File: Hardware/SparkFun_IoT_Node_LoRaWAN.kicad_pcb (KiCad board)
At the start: 4 copper layers, 59 x 82 mm, 102 parts, among them J1 Conn_01x03, J2 JST_2mm_LiPo, J3 Qwiic_RA, J4 USB_C_Receptacle, J5 USB_C_Receptacle, J6 SWD, J7 Conn_01x12, J8 Conn_01x12, J9 microSD_Friction, SW1 SMD_4.6x2.8mm_h2.5mm, SW2 SMD_4.6x2.8mm_h2.5mm, SW3 DPDT_Slide_SMD_7.2x3.5mm, SW4 PTH_RA_h7.5mm, U3 CH340C, U4 W25Q128JVPIM, U5 LM66200, U6 RT9080-3.3, U7 MCP73831, U8 MAX17048, U9 RT9080-3.3

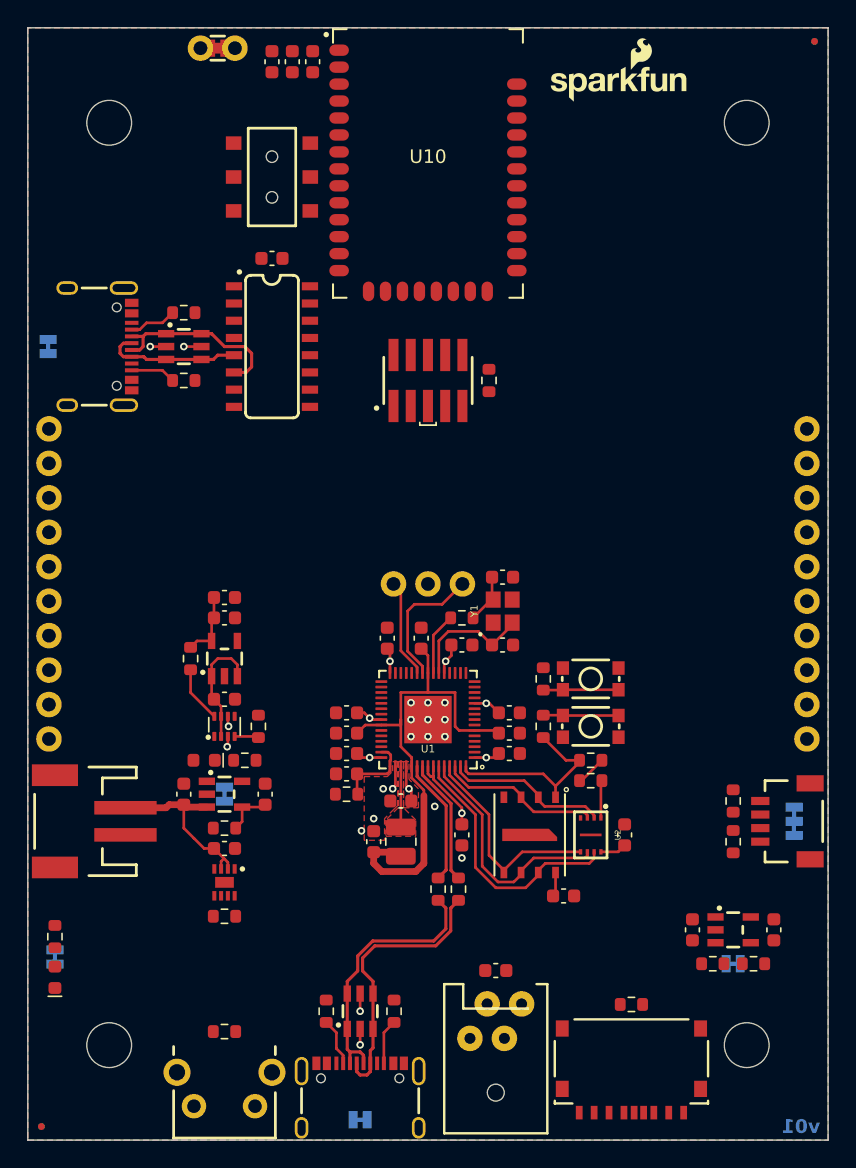
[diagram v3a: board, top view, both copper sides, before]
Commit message: Finish connections and routing
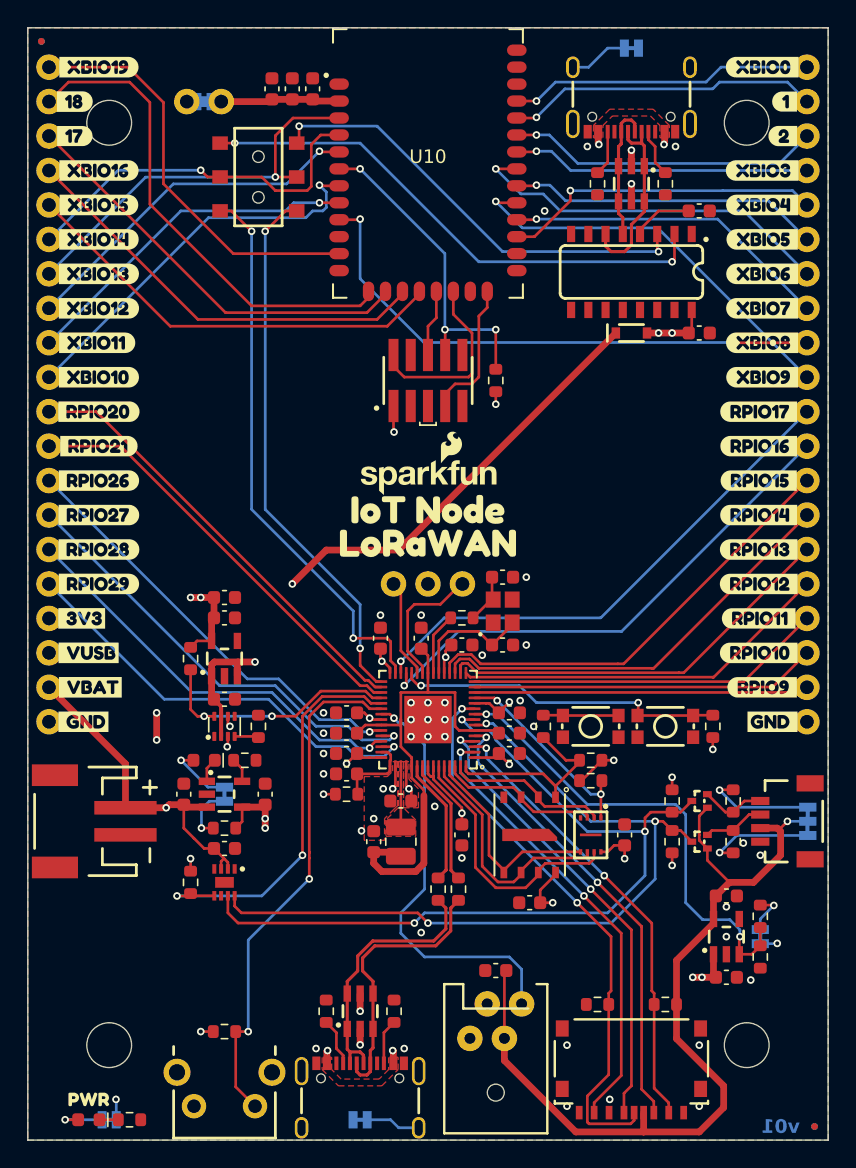
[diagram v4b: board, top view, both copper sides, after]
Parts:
- added C31: 0.1uF, SparkFun-Capacitor:C_0603_1608Metric, F.Cu at (120.0, 81.5)
- added D6: BAT20J, SparkFun-Semiconductor-Standard:SOD-323, F.Cu at (115.0, 81.5)
- added G***: LOGO, SparkFun-Aesthetic:SparkFun_Logo_10mm, B.Cu at (100.0, 85.0)
- added Q1: RE1C002UNTCL, SparkFun-Semiconductor-Standard:SC-89 SOT-490, F.Cu at (119.5, 119.0)
- added Q2: RE1C002UNTCL, SparkFun-Semiconductor-Standard:SC-89 SOT-490, F.Cu at (119.5, 116.0)
- added R26: 10k, SparkFun-Resistor:R_0603_1608Metric, F.Cu at (117.5, 131.0)
- added R27: 2.2k, SparkFun-Resistor:R_0603_1608Metric, F.Cu at (118.0, 116.0)
- added R28: 2.2k, SparkFun-Resistor:R_0603_1608Metric, F.Cu at (118.0, 119.0)
- added kibuzzard-6691B276: G***, kibuzzard-6691B276, F.Cu at (74.6, 110.2)
- added kibuzzard-6691B276: G***, kibuzzard-6691B276, B.Cu at (125.4, 110.2)
- added kibuzzard-6691B276: G***, kibuzzard-6691B276, B.Cu at (100.0, 97.5)
- added kibuzzard-6691B296: G***, kibuzzard-6691B296, F.Cu at (75.1, 107.6)
- added kibuzzard-6691B29E: G***, kibuzzard-6691B29E, F.Cu at (75.0, 105.1)
- added kibuzzard-6691B2AD: G***, kibuzzard-6691B2AD, F.Cu at (74.5, 102.5)
- added kibuzzard-6691B2C0: G***, kibuzzard-6691B2C0, F.Cu at (75.7, 100.0)
- added kibuzzard-6691B2FA: G***, kibuzzard-6691B2FA, F.Cu at (75.7, 97.5)
- added kibuzzard-6691B2FE: G***, kibuzzard-6691B2FE, F.Cu at (75.7, 94.9)
- added kibuzzard-6691B304: G***, kibuzzard-6691B304, F.Cu at (75.7, 92.4)
- added kibuzzard-6691B307: G***, kibuzzard-6691B307, F.Cu at (75.7, 89.8)
- added kibuzzard-6691B30B: G***, kibuzzard-6691B30B, F.Cu at (75.7, 87.3)
- added kibuzzard-6691B338: G***, kibuzzard-6691B338, F.Cu at (124.4, 87.3)
- added kibuzzard-6691B363: G***, kibuzzard-6691B363, F.Cu at (124.4, 100.0)
- added kibuzzard-6691B36B: G***, kibuzzard-6691B36B, F.Cu at (124.4, 89.8)
- added kibuzzard-6691B36F: G***, kibuzzard-6691B36F, F.Cu at (124.4, 92.4)
- added kibuzzard-6691B376: G***, kibuzzard-6691B376, F.Cu at (124.4, 94.9)
- added kibuzzard-6691B37B: G***, kibuzzard-6691B37B, F.Cu at (124.4, 97.5)
- added kibuzzard-6691B383: G***, kibuzzard-6691B383, F.Cu at (124.4, 102.5)
- added kibuzzard-6691B387: G***, kibuzzard-6691B387, F.Cu at (124.4, 105.1)
- added kibuzzard-6691B38E: G***, kibuzzard-6691B38E, F.Cu at (124.6, 107.6)
- added kibuzzard-6691B3A2: G***, kibuzzard-6691B3A2, F.Cu at (125.4, 110.2)
- added kibuzzard-6691B3A2: G***, kibuzzard-6691B3A2, B.Cu at (74.6, 110.2)
- added kibuzzard-6691B3CB: G***, kibuzzard-6691B3CB, F.Cu at (75.7, 84.8)
- added kibuzzard-6691B3E1: G***, kibuzzard-6691B3E1, F.Cu at (75.7, 61.9)
- added kibuzzard-6691B3E7: G***, kibuzzard-6691B3E7, F.Cu at (75.7, 69.5)
- added kibuzzard-6691B3EC: G***, kibuzzard-6691B3EC, F.Cu at (75.7, 72.1)
- added kibuzzard-6691B3F1: G***, kibuzzard-6691B3F1, F.Cu at (75.7, 74.6)
- added kibuzzard-6691B3F5: G***, kibuzzard-6691B3F5, F.Cu at (75.7, 77.1)
- added kibuzzard-6691B3F9: G***, kibuzzard-6691B3F9, F.Cu at (75.7, 79.7)
- added kibuzzard-6691B3FD: G***, kibuzzard-6691B3FD, F.Cu at (75.6, 82.2)
- added kibuzzard-6691B419: G***, kibuzzard-6691B419, F.Cu at (124.6, 84.8)
- added kibuzzard-6691B436: G***, kibuzzard-6691B436, F.Cu at (124.6, 61.9)
- added kibuzzard-6691B43C: G***, kibuzzard-6691B43C, F.Cu at (124.6, 69.5)
- added kibuzzard-6691B440: G***, kibuzzard-6691B440, F.Cu at (124.6, 72.1)
- added kibuzzard-6691B444: G***, kibuzzard-6691B444, F.Cu at (124.6, 74.6)
- added kibuzzard-6691B448: G***, kibuzzard-6691B448, F.Cu at (124.6, 77.1)
- added kibuzzard-6691B44C: G***, kibuzzard-6691B44C, F.Cu at (124.6, 79.7)
- added kibuzzard-6691B450: G***, kibuzzard-6691B450, F.Cu at (124.6, 82.2)
- added kibuzzard-6691B464: G***, kibuzzard-6691B464, F.Cu at (126.2, 67.0)
- added kibuzzard-6691B472: G***, kibuzzard-6691B472, F.Cu at (126.3, 64.4)
- added kibuzzard-6691B480: G***, kibuzzard-6691B480, F.Cu at (74.0, 67.0)
- added kibuzzard-6691B48E: G***, kibuzzard-6691B48E, F.Cu at (74.0, 64.4)
- added kibuzzard-6691B4B8: G***, kibuzzard-6691B4B8, F.Cu at (100.0, 94.5)
- added kibuzzard-6691B4B8: G***, kibuzzard-6691B4B8, B.Cu at (100.0, 87.5)
- added kibuzzard-6691B4CC: G***, kibuzzard-6691B4CC, F.Cu at (100.0, 97.0)
- added kibuzzard-6691B4CC: G***, kibuzzard-6691B4CC, B.Cu at (100.0, 90.0)
- added kibuzzard-6691B525: G***, kibuzzard-6691B525, B.Cu at (75.7, 87.3)
- added kibuzzard-6691B54A: G***, kibuzzard-6691B54A, B.Cu at (75.7, 89.8)
- added kibuzzard-6691B55C: G***, kibuzzard-6691B55C, B.Cu at (75.7, 92.4)
- added kibuzzard-6691B561: G***, kibuzzard-6691B561, B.Cu at (75.7, 94.9)
- added kibuzzard-6691B566: G***, kibuzzard-6691B566, B.Cu at (75.7, 97.5)
- added kibuzzard-6691B56B: G***, kibuzzard-6691B56B, B.Cu at (75.7, 100.0)
- added kibuzzard-6691B580: G***, kibuzzard-6691B580, B.Cu at (124.4, 87.3)
- added kibuzzard-6691B59B: G***, kibuzzard-6691B59B, B.Cu at (124.6, 107.6)
- added kibuzzard-6691B5A1: G***, kibuzzard-6691B5A1, B.Cu at (124.4, 105.1)
- added kibuzzard-6691B5A6: G***, kibuzzard-6691B5A6, B.Cu at (124.4, 102.5)
- added kibuzzard-6691B5AC: G***, kibuzzard-6691B5AC, B.Cu at (124.4, 100.0)
- added kibuzzard-6691B5B1: G***, kibuzzard-6691B5B1, B.Cu at (124.4, 97.5)
- added kibuzzard-6691B5BB: G***, kibuzzard-6691B5BB, B.Cu at (124.4, 94.9)
- added kibuzzard-6691B5C0: G***, kibuzzard-6691B5C0, B.Cu at (124.4, 92.4)
- added kibuzzard-6691B5C3: G***, kibuzzard-6691B5C3, B.Cu at (124.4, 89.8)
- added kibuzzard-6691B5E6: G***, kibuzzard-6691B5E6, B.Cu at (74.5, 102.5)
- added kibuzzard-6691B5F0: G***, kibuzzard-6691B5F0, B.Cu at (75.0, 105.1)
- added kibuzzard-6691B5FB: G***, kibuzzard-6691B5FB, B.Cu at (75.1, 107.6)
- added kibuzzard-6691B60A: G***, kibuzzard-6691B60A, B.Cu at (124.6, 84.8)
- added kibuzzard-6691B61F: G***, kibuzzard-6691B61F, B.Cu at (124.6, 61.9)
- added kibuzzard-6691B623: G***, kibuzzard-6691B623, B.Cu at (124.6, 69.5)
- added kibuzzard-6691B627: G***, kibuzzard-6691B627, B.Cu at (124.6, 72.1)
- added kibuzzard-6691B62B: G***, kibuzzard-6691B62B, B.Cu at (124.6, 74.6)
- added kibuzzard-6691B62F: G***, kibuzzard-6691B62F, B.Cu at (124.6, 77.1)
- added kibuzzard-6691B633: G***, kibuzzard-6691B633, B.Cu at (124.6, 79.7)
- added kibuzzard-6691B637: G***, kibuzzard-6691B637, B.Cu at (124.6, 82.2)
- added kibuzzard-6691B641: G***, kibuzzard-6691B641, B.Cu at (126.2, 67.0)
- added kibuzzard-6691B649: G***, kibuzzard-6691B649, B.Cu at (126.3, 64.4)
- added kibuzzard-6691B658: G***, kibuzzard-6691B658, B.Cu at (74.0, 67.0)
- added kibuzzard-6691B661: G***, kibuzzard-6691B661, B.Cu at (74.0, 64.4)
- added kibuzzard-6691B670: G***, kibuzzard-6691B670, B.Cu at (75.7, 69.5)
- added kibuzzard-6691B697: G***, kibuzzard-6691B697, B.Cu at (75.7, 61.9)
- added kibuzzard-6691B6A1: G***, kibuzzard-6691B6A1, B.Cu at (75.7, 72.1)
- added kibuzzard-6691B6A6: G***, kibuzzard-6691B6A6, B.Cu at (75.7, 74.6)
- added kibuzzard-6691B6AB: G***, kibuzzard-6691B6AB, B.Cu at (75.7, 77.1)
- added kibuzzard-6691B6B0: G***, kibuzzard-6691B6B0, B.Cu at (75.7, 79.7)
- added kibuzzard-6691B6B5: G***, kibuzzard-6691B6B5, B.Cu at (75.6, 82.2)
- added kibuzzard-6691B6B9: G***, kibuzzard-6691B6B9, B.Cu at (75.7, 84.8)
- added kibuzzard-6691B6EC: G***, kibuzzard-6691B6EC, B.Cu at (83.5, 66.1)
- added kibuzzard-6691B712: G***, kibuzzard-6691B712, B.Cu at (95.0, 137.8)
- added kibuzzard-6691B712: G***, kibuzzard-6691B712, B.Cu at (115.0, 62.2)
- added kibuzzard-6691B72F: G***, kibuzzard-6691B72F, B.Cu at (76.5, 137.8)
- added kibuzzard-6691B73B: G***, kibuzzard-6691B73B, B.Cu at (126.2, 117.5)
- added kibuzzard-6691B750: G***, kibuzzard-6691B750, B.Cu at (126.2, 126.0)
- added kibuzzard-6691B763: G***, kibuzzard-6691B763, B.Cu at (86.8, 115.5)
- added kibuzzard-6691B7AB: G***, kibuzzard-6691B7AB, B.Cu at (102.5, 96.3)
- added kibuzzard-6691B7BF: G***, kibuzzard-6691B7BF, B.Cu at (97.5, 96.4)
- added kibuzzard-6691B872: G***, kibuzzard-6691B872, F.Cu at (75.0, 138.0)
- J7, J8: footprint SparkFun-Connector:1x10 -> SparkFun-Connector:1x20
- JP6: moved to B.Cu
- moved FID1 57.0 mm to (71.5, 60.0)
- moved FID2 57.0 mm to (128.5, 140.0)
- moved FID3 57.0 mm to (71.5, 60.0)
- moved FID4 57.0 mm to (128.5, 140.0)
- moved J7 49.5 mm to (72.1, 61.9), turned to -90 degrees
- moved J8 49.5 mm to (127.9, 61.9), turned to -90 degrees
- moved JP5 48.3 mm to (115.0, 60.5), turned to 0 degrees
- moved J4 39.7 mm to (115.0, 67.0), turned to 180 degrees
- moved R18 36.7 mm to (117.5, 70.5), turned to -90 degrees
- moved D5 35.1 mm to (115.0, 70.5), turned to -90 degrees
- moved R17 33.8 mm to (112.5, 70.5), turned to -90 degrees
- moved G*** 32.2 mm to (100.0, 92.0)
- moved C27 31.7 mm to (120.0, 72.5), turned to 0 degrees
- moved U3 27.1 mm to (115.0, 77.0), turned to -90 degrees
- moved R10 14.6 mm to (78.0, 139.5), turned to 0 degrees
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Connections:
- C27 pad 1: 3.3V -> V3
- C4 pad 1: VBUS -> VUSB
- D3 pad 1: GND -> Net-(D3-K)
- D4 pad 5: VBUS -> VUSB
- D5 pad 5: VBUS -> VUSB_2
- J3 pad 3: SDA -> SDA_OUT
- J3 pad 4: SCL -> SCL_OUT
- J4 pad VBUS: VBUS -> VUSB_2
- J5 pad VBUS: VBUS -> VUSB
- J6 pad 10: XBLR_~{RESET} -> (no net)
- J6 pad 2: XBLR_SWDIO -> XBLR_SWO
- J6 pad 3: GND -> (no net)
- J6 pad 4: XBLR_SWCLK -> (no net)
- J6 pad 6: XBLR_SWO -> XBLR_SWCLK
- J6 pad 7: (no net) -> XBLR_SWDIO
- J6 pad 8: (no net) -> XBLR_~{RESET}
- J6 pad 9: GND -> (no net)
- J7 pad 1: unconnected-(J7-Pin_1-Pad1) -> XBLR_IO19
- J7 pad 10: unconnected-(J7-Pin_10-Pad10) -> XBLR_IO10
- J7 pad 2: unconnected-(J7-Pin_2-Pad2) -> XBLR_IO18
- J7 pad 3: unconnected-(J7-Pin_3-Pad3) -> XBLR_IO17
- J7 pad 4: unconnected-(J7-Pin_4-Pad4) -> XBLR_IO16
- J7 pad 5: unconnected-(J7-Pin_5-Pad5) -> XBLR_IO15
- J7 pad 6: unconnected-(J7-Pin_6-Pad6) -> XBLR_RX/IO14
- J7 pad 7: unconnected-(J7-Pin_7-Pad7) -> XBLR_TX/IO13
- J7 pad 8: unconnected-(J7-Pin_8-Pad8) -> XBLR_IO12
- J7 pad 9: unconnected-(J7-Pin_9-Pad9) -> XBLR_IO11
- J8 pad 1: unconnected-(J8-Pin_1-Pad1) -> XBLR_IO0
- J8 pad 10: unconnected-(J8-Pin_10-Pad10) -> XBLR_IO9
- J8 pad 2: unconnected-(J8-Pin_2-Pad2) -> XBLR_IO1
- J8 pad 3: unconnected-(J8-Pin_3-Pad3) -> XBLR_IO2
- J8 pad 4: unconnected-(J8-Pin_4-Pad4) -> XBLR_IO3
- J8 pad 5: unconnected-(J8-Pin_5-Pad5) -> XBLR_IO4
- J8 pad 6: unconnected-(J8-Pin_6-Pad6) -> XBLR_IO5
- J8 pad 7: unconnected-(J8-Pin_7-Pad7) -> XBLR_IO6
- J8 pad 8: unconnected-(J8-Pin_8-Pad8) -> XBLR_IO7
- J8 pad 9: unconnected-(J8-Pin_9-Pad9) -> XBLR_IO8
- JP3 pad 1: Net-(JP3-A) -> Net-(D3-A)
- R10 pad 1: Net-(JP3-A) -> Net-(D3-K)
- R10 pad 2: Net-(D3-A) -> GND
- R13 pad 2: SDA -> SDA_OUT
- R20 pad 2: SCL -> SCL_OUT
- R9 pad 1: VBUS -> VUSB
- SW3 pad 2: XBLR_RX -> XBLR_RX/IO14
- SW3 pad 5: XBLR_TX -> XBLR_TX/IO13
- U1 pad 10: unconnected-(U1-GPIO7-Pad10) -> SD_DET
- U1 pad 12: unconnected-(U1-GPIO8-Pad12) -> PSRAM_~{CS}
- U1 pad 13: unconnected-(U1-GPIO9-Pad13) -> RP2350_IO9
- U1 pad 14: unconnected-(U1-GPIO10-Pad14) -> RP2350_IO10
- U1 pad 15: unconnected-(U1-GPIO11-Pad15) -> RP2350_IO11
- U1 pad 16: unconnected-(U1-GPIO12-Pad16) -> RP2350_IO12
- U1 pad 17: unconnected-(U1-GPIO13-Pad17) -> RP2350_IO13
- U1 pad 18: unconnected-(U1-GPIO14-Pad18) -> RP2350_IO14
- U1 pad 19: unconnected-(U1-GPIO15-Pad19) -> RP2350_IO15
- U1 pad 2: unconnected-(U1-GPIO0-Pad2) -> SD_POCI
- U1 pad 27: unconnected-(U1-GPIO16-Pad27) -> RP2350_IO16
- U1 pad 28: unconnected-(U1-GPIO17-Pad28) -> RP2350_IO17
- U1 pad 29: unconnected-(U1-GPIO18-Pad29) -> RP2350_TX
- U1 pad 3: unconnected-(U1-GPIO1-Pad3) -> SD_~{CS}
- U1 pad 31: unconnected-(U1-GPIO19-Pad31) -> RP2350_RX
- U1 pad 32: unconnected-(U1-GPIO20-Pad32) -> RP2350_IO20
- U1 pad 33: unconnected-(U1-GPIO21-Pad33) -> RP2350_IO21
- U1 pad 34: unconnected-(U1-GPIO22-Pad34) -> BAT_POWER
- U1 pad 35: unconnected-(U1-GPIO23-Pad35) -> FUEL_GAUGE_~{ALRT}
- U1 pad 36: unconnected-(U1-GPIO24-Pad36) -> USER_BUTTON
- U1 pad 37: unconnected-(U1-GPIO25-Pad37) -> LED_IN
- U1 pad 4: unconnected-(U1-GPIO2-Pad4) -> SD_SCK
- U1 pad 40: unconnected-(U1-GPIO26/ADC0-Pad40) -> RP2350_IO26
- U1 pad 41: unconnected-(U1-GPIO27/ADC1-Pad41) -> RP2350_IO27
- U1 pad 42: unconnected-(U1-GPIO28/ADC2-Pad42) -> RP2350_IO28
- U1 pad 43: unconnected-(U1-GPIO29/ADC3-Pad43) -> RP2350_IO29
- U1 pad 5: unconnected-(U1-GPIO3-Pad5) -> SD_PICO
- U1 pad 7: unconnected-(U1-GPIO4-Pad7) -> SDA
- U1 pad 8: unconnected-(U1-GPIO5-Pad8) -> SCL
- U1 pad 9: unconnected-(U1-GPIO6-Pad9) -> PERIPHERAL_POWER
- U10 pad 11: unconnected-(U10-~{ATTN}/DIO19-Pad11) -> XBLR_IO19
- U10 pad 13: unconnected-(U10-SPI_SCLK/DIO18-Pad13) -> XBLR_IO18
- U10 pad 14: unconnected-(U10-SPI_~{SSEL}/DIO17-Pad14) -> XBLR_IO17
- U10 pad 15: unconnected-(U10-SPI_MOSI/DIO16-Pad15) -> XBLR_IO16
- U10 pad 16: unconnected-(U10-SPI_MISO/DIO15-Pad16) -> XBLR_IO15
- U10 pad 23: unconnected-(U10-DIO4-Pad23) -> XBLR_IO4
- U10 pad 24: unconnected-(U10-~{CTS}/DIO7-Pad24) -> XBLR_IO7
- U10 pad 25: unconnected-(U10-ON/~{SLP}/DIO9-Pad25) -> XBLR_IO9
- U10 pad 26: unconnected-(U10-ASSOC/DIO5-Pad26) -> XBLR_IO5
- U10 pad 27: unconnected-(U10-~{RTS}/DIO6-Pad27) -> XBLR_IO6
- U10 pad 28: unconnected-(U10-AD3/DIO3-Pad28) -> XBLR_IO3
- U10 pad 29: unconnected-(U10-AD2/DIO2-Pad29) -> XBLR_IO2
- U10 pad 3: XBLR_TX -> XBLR_TX/IO13
- U10 pad 30: unconnected-(U10-AD1/DIO1-Pad30) -> XBLR_IO1
- U10 pad 31: unconnected-(U10-COMM/AD0/DIO0-Pad31) -> XBLR_IO0
- U10 pad 4: XBLR_RX -> XBLR_RX/IO14
- U10 pad 5: unconnected-(U10-DIO12-Pad5) -> XBLR_IO12
- U10 pad 7: unconnected-(U10-PWM0/RSSI/DIO10-Pad7) -> XBLR_IO10
- U10 pad 8: unconnected-(U10-PWM1/DIO11-Pad8) -> XBLR_IO11
- U10 pad 9: unconnected-(U10-~{DTR}/DIO8-Pad9) -> XBLR_IO8
- U3 pad 16: 3.3V -> VUSB_2
- U3 pad 4: 3.3V -> V3
- U5 pad 6: VBUS -> VUSB
- U7 pad 4: VBUS -> VUSB
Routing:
- net VUSB: track 0.00 -> 93.9 mm, vias 0 -> 7
- net 3.3V_P: track 0.00 -> 63.9 mm, vias 0 -> 1
- net SCL: track 0.00 -> 60.0 mm, vias 0 -> 3
- net SDA: track 0.00 -> 57.5 mm, vias 0 -> 3
- net VIN: track 8.70 -> 64.2 mm, vias 0 -> 3
- net SD_DET: track 0.00 -> 41.5 mm, vias 0 -> 2
- net RP2350_TX: track 0.00 -> 41.4 mm, vias 0 -> 2
- net XBLR_IO8: track 0.00 -> 40.9 mm, vias 0 -> 2
- net RP2350_RX: track 0.00 -> 39.9 mm, vias 0 -> 2
- net XBLR_USB_TX: track 0.00 -> 39.1 mm, vias 0 -> 2
- net RP2350_IO17: track 0.00 -> 38.4 mm, vias 0 -> 1
- net USER_BUTTON: track 0.00 -> 38.1 mm, vias 0 -> 2
- net RP2350_IO16: track 0.00 -> 38.0 mm, vias 0 -> 1
- net XBLR_IO18: track 0.00 -> 36.1 mm
- net PERIPHERAL_POWER: track 0.00 -> 34.9 mm, vias 0 -> 2
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- added copper zone on F.Cu, net VUSB
- added copper zone on In2.Cu, net VUSB
- added copper zone on F.Cu, net VUSB_2
- added copper zone on In2.Cu, net VUSB_2
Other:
- board text added: "Finish: Lead Free HASL"
- board text removed: "Finish: ENIG"

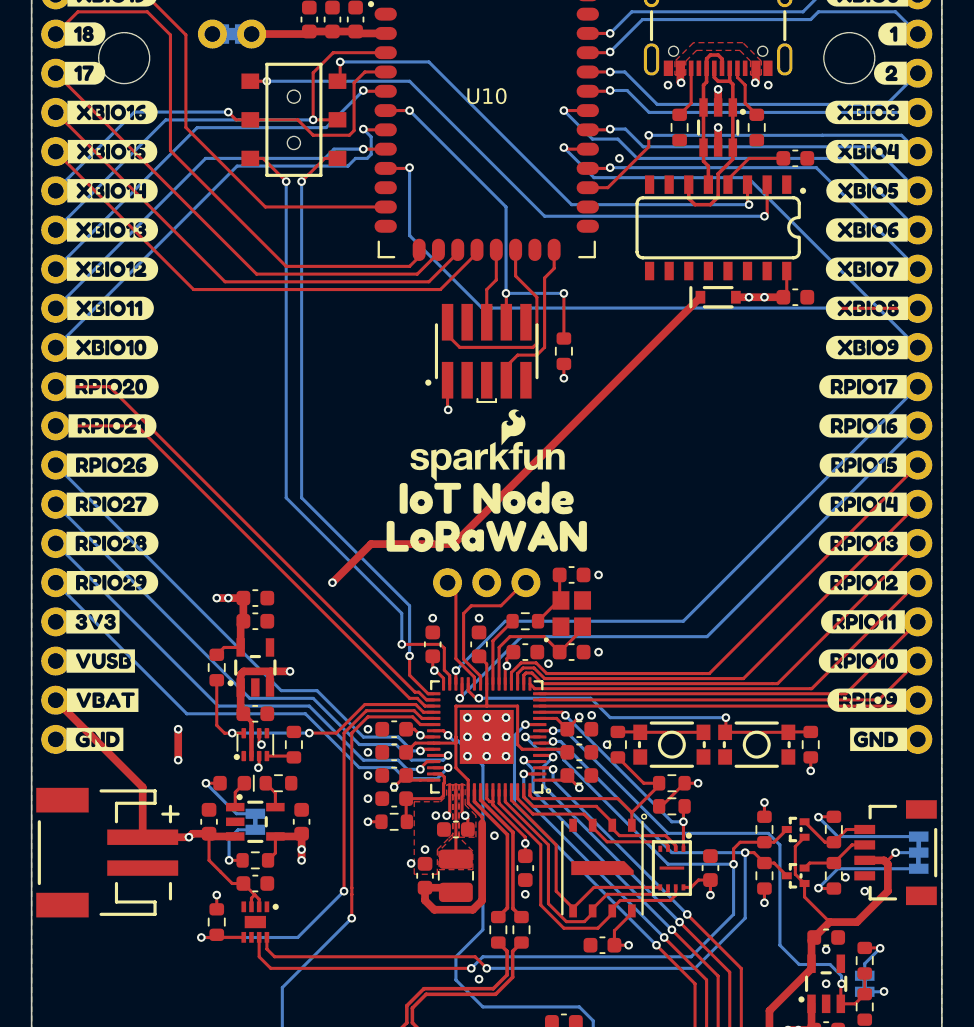
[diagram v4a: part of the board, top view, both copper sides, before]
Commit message: Add silk labels to UART switch
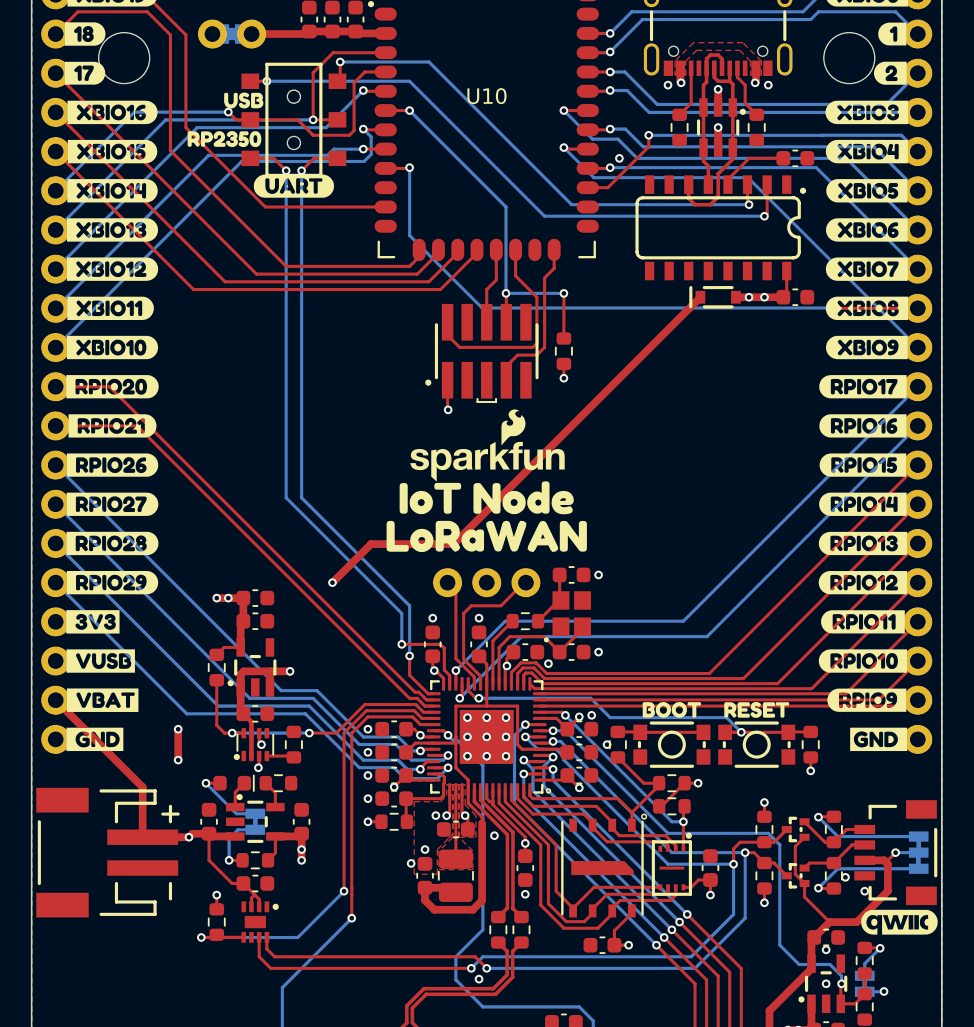
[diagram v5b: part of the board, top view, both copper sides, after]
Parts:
- added G***: LOGO, SparkFun-Aesthetic:qwiic_5mm, F.Cu at (126.8, 122.0)
- added kibuzzard-6691B8D3: G***, kibuzzard-6691B8D3, F.Cu at (112.0, 108.2)
- added kibuzzard-6691B8DD: G***, kibuzzard-6691B8DD, F.Cu at (117.5, 108.2)
- added kibuzzard-6691B926: G***, kibuzzard-6691B926, F.Cu at (83.0, 71.2)
- added kibuzzard-6691B931: G***, kibuzzard-6691B931, F.Cu at (84.2, 68.8)
- added kibuzzard-6691B952: G***, kibuzzard-6691B952, F.Cu at (87.5, 74.3)
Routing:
- net ~{RESET}: track 24.4 -> 25.9 mm

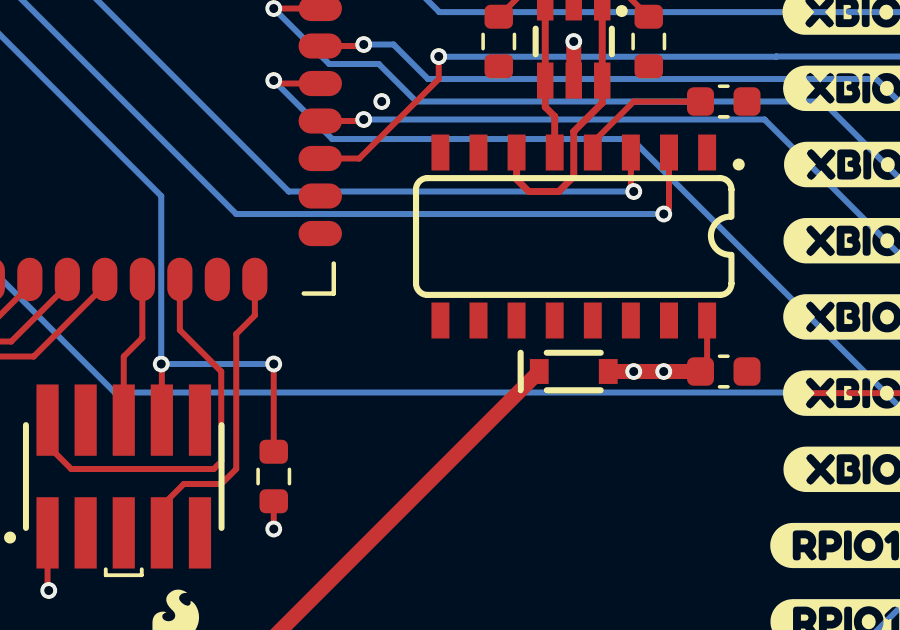
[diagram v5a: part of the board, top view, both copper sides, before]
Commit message: Add level shifter to CH340 TX pin
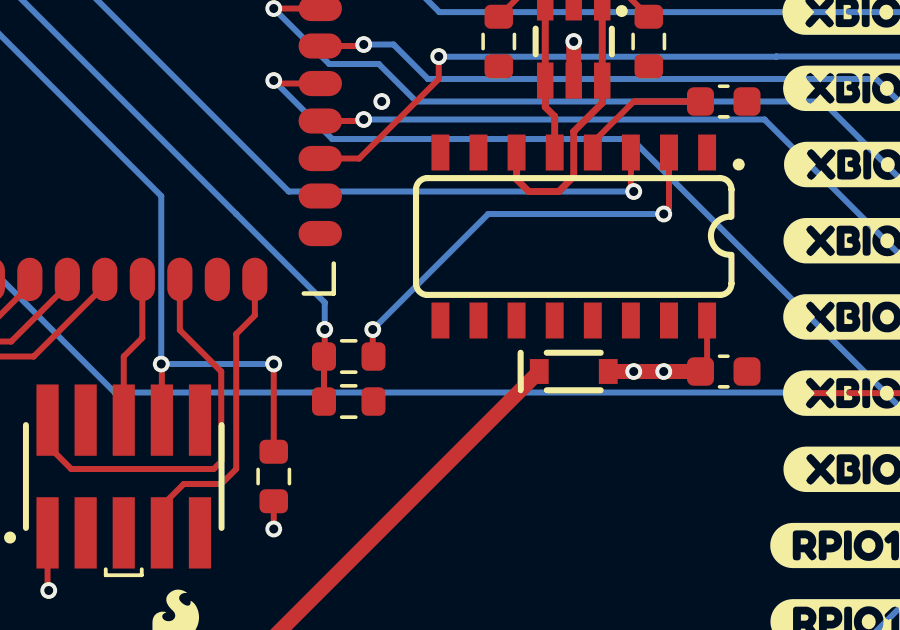
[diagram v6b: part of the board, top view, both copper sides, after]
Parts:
- added R29: 5.1k, SparkFun-Resistor:R_0603_1608Metric, F.Cu at (107.5, 81.0)
- added R30: 10k, SparkFun-Resistor:R_0603_1608Metric, F.Cu at (107.5, 82.5)
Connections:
- U3 pad 2: XBLR_USB_TX -> Net-(U3-TXD)
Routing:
- net Net-(U3-TXD): track 0.00 -> 14.3 mm, vias 0 -> 2
- net XBLR_USB_TX: track 39.1 -> 30.2 mm

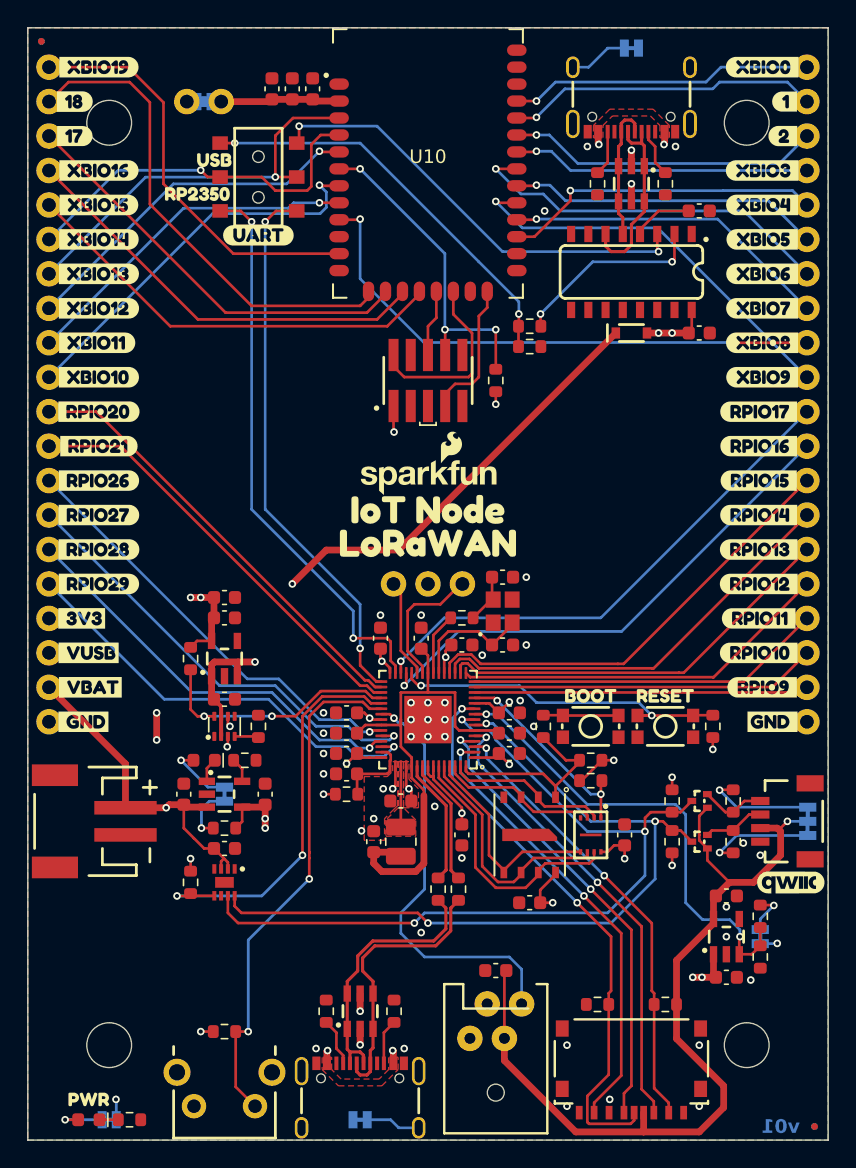
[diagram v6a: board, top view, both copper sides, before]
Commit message: Improve GND stitching
Add lots of GND vias
Nudge tracks to connect GND pour regions
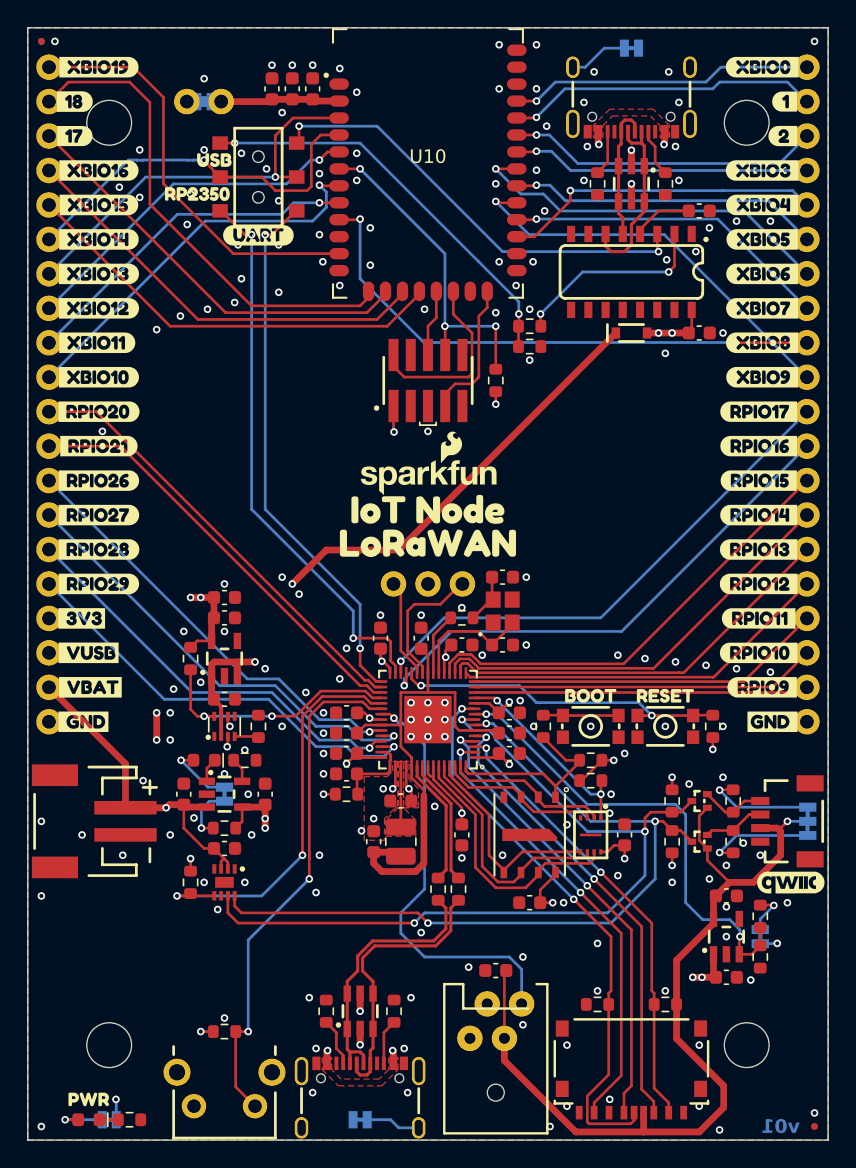
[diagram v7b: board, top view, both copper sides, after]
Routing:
- net XBLR_RX/IO14: track 27.6 -> 28.3 mm
- net RP2350_RX: track 40.3 -> 39.8 mm
- net RP2350_TX: track 41.8 -> 41.2 mm
- net GND: vias 44 -> 175
